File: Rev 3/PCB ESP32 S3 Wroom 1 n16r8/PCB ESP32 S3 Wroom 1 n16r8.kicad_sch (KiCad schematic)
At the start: 28 parts, among them J1 AudioJack3_SwitchT, M1 Haptic Feedback, Q1 BS170, SW1 Home, SW2 Back, SW3 Play/Pause, SW4 Power, SW5 Menu, SW6 Hold, U1 Wemos Lolin32 Lite

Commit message: began work on rev 3
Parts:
- removed U1: Wemos Lolin32 Lite, MP3_Player_Custom_Footprints:Wemos Lolin32 Lite v1.0.0, symbol MP3_Player_Custom_Parts:Wemos Lolin32 Lite
- added X1: ESP32-S3-WROOM-1-N16R8, MP3_Player_Custom_Footprints:ESP32S3WROOM1N8R2, symbol ESP32-S3-WROOM-1-N16R8:ESP32-S3-WROOM-1-N16R8
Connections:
- net GND: now also X1.1 (GND), X1.40 (GND), X1.41 (GND), X1.42 (GND), X1.43 (GND), X1.44 (GND), X1.45 (GND), X1.46 (GND), X1.47 (GND), X1.48 (GND), X1.49 (GND)
- net VDD: now also X1.2 (3V3)

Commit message: wired up ESP32 to the best of my knowledge
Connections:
- net DAC_BCLK: now also X1.5 (IO5)
- net DAC_DIN: now also X1.4 (IO4)
- net DAC_LRC: now also X1.6 (IO6)
- net Detect_Jack: now also X1.15 (IO3)
- net Gain: now also X1.8 (IO15)
- net Motor_Driver: now also X1.11 (IO18)
- net RESET: now also X1.3 (EN)
- net SCREEN_BRIGHTNESS: now also X1.10 (IO17)
- net SD_CS: now also X1.38 (IO2)
- net SPI_MISO: now also X1.20 (IO12)
- net SPI_MOSI: now also X1.21 (IO13)
- net SPI_SCK: now also X1.22 (IO14)
- net TFT_CS: now also X1.39 (IO1)
- net TFT_DC: now also X1.17 (IO9)
- net at Primary Rotary Encoder1.A, R2.1: now also X1.7 (IO7)
- net at R4.2, SW3.2 (B): now also X1.14 (IO20)
- net at X1.12 (IO8): now also SW6.2 (B)
- net at X1.13 (IO19): now also R5.2, R6.2, SW2.1 (A), SW5.2 (B), X1.19 (IO11)
- net at X1.18 (IO10): now also R3.2, SW1.1 (A)
- net at X1.9 (IO16): now also Primary Rotary Encoder1.B, R1.1
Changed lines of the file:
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@@
 	)
 	(junction
+		(at 149.86 72.39)
+		(diameter 0)
+		(color 0 0 0 0)
+	)
+	(junction
 		(at 243.84 129.54)
 		(diameter 0)
@@
 	)
 	(junction
+		(at 149.86 68.58)
+		(diameter 0)
+		(color 0 0 0 0)
+	)
+	(junction
 		(at 149.86 62.23)
 		(diameter 0)
@@
 	(wire
 		(pts
-			(xy 82.55 64.77) (xy 113.03 64.77)
+			(xy 72.39 64.77) (xy 102.87 64.77)
 		)
 		(stroke
@@
 	(wire
 		(pts
-			(xy 160.02 68.58) (xy 195.58 68.58)
+			(xy 149.86 68.58) (xy 195.58 68.58)
 		)
 		(stroke
@@
 	(wire
 		(pts
-			(xy 97.79 85.09) (xy 82.55 85.09)
+			(xy 87.63 85.09) (xy 72.39 85.09)
 		)
 		(stroke
@@
 	(wire
 		(pts
-			(xy 113.03 64.77) (xy 113.03 45.72)
+			(xy 102.87 64.77) (xy 102.87 63.5)
 		)
 		(stroke
@@
 	(wire
 		(pts
-			(xy 139.7 45.72) (xy 139.7 87.63)
+			(xy 129.54 45.72) (xy 129.54 69.85)
 		)
 		(stroke
@@
 	(wire
 		(pts
-			(xy 170.18 73.66) (xy 170.18 95.25)
+			(xy 160.02 73.66) (xy 160.02 95.25)
 		)
 		(stroke
@@
 	(wire
 		(pts
-			(xy 96.52 62.23) (xy 82.55 62.23)
+			(xy 86.36 62.23) (xy 72.39 62.23)
 		)
 		(stroke
@@
 	(wire
 		(pts
-			(xy 97.79 15.24) (xy 228.6 15.24)
+			(xy 87.63 15.24) (xy 228.6 15.24)
 		)
 		(stroke
@@
 	(wire
 		(pts
-			(xy 82.55 90.17) (xy 149.86 90.17)
+			(xy 72.39 72.39) (xy 149.86 72.39)
 		)
 		(stroke
@@
 	(wire
 		(pts
-			(xy 82.55 95.25) (xy 170.18 95.25)
+			(xy 72.39 95.25) (xy 160.02 95.25)
 		)
 		(stroke
@@
 	(wire
 		(pts
-			(xy 170.18 73.66) (xy 203.2 73.66)
+			(xy 160.02 73.66) (xy 203.2 73.66)
 		)
 		(stroke
@@
 	(wire
 		(pts
-			(xy 82.55 92.71) (xy 160.02 92.71)
+			(xy 113.03 63.5) (xy 113.03 45.72)
+		)
+		(stroke
+			(width 0)
+			(type default)
+		)
+	)
+	(wire
+		(pts
+			(xy 72.39 92.71) (xy 149.86 92.71)
 		)
 		(stroke
@@
 	(wire
 		(pts
-			(xy 82.55 87.63) (xy 139.7 87.63)
+			(xy 72.39 69.85) (xy 129.54 69.85)
 		)
 		(stroke
@@
 	(wire
 		(pts
-			(xy 96.52 13.97) (xy 248.92 13.97)
+			(xy 86.36 13.97) (xy 248.92 13.97)
 		)
 		(stroke
@@
 	(wire
 		(pts
-			(xy 149.86 45.72) (xy 139.7 45.72)
+			(xy 149.86 45.72) (xy 129.54 45.72)
 		)
 		(stroke
@@
 	(wire
 		(pts
-			(xy 96.52 13.97) (xy 96.52 62.23)
+			(xy 86.36 13.97) (xy 86.36 62.23)
 		)
 		(stroke
@@
 	(wire
 		(pts
+			(xy 149.86 72.39) (xy 149.86 92.71)
+		)
+		(stroke
+			(width 0)
+			(type default)
+		)
+	)
+	(wire
+		(pts
 			(xy 142.24 135.89) (xy 147.32 135.89)
 		)
@@
 	(wire
 		(pts
-			(xy 160.02 68.58) (xy 160.02 92.71)
+			(xy 149.86 68.58) (xy 149.86 72.39)
 		)
 		(stroke
@@
 	(wire
 		(pts
-			(xy 97.79 15.24) (xy 97.79 85.09)
+			(xy 87.63 15.24) (xy 87.63 85.09)
 		)
 		(stroke
@@
 	(wire
 		(pts
+			(xy 102.87 63.5) (xy 113.03 63.5)
+		)
+		(stroke
+			(width 0)
+			(type default)
+		)
+	)
+	(wire
+		(pts
 			(xy 242.57 25.4) (xy 248.92 25.4)
 		)
@@
 	(wire
 		(pts
-			(xy 149.86 62.23) (xy 149.86 90.17)
+			(xy 228.6 50.8) (xy 228.6 25.4)
 		)
 		(stroke
 			(width 0)
 			(type default)
+			(color 57 191 251 1)
 		)
 	)
 	(wire
 		(pts
-			(xy 228.6 50.8) (xy 228.6 25.4)
+			(xy 149.86 68.58) (xy 149.86 62.23)
 		)
 		(stroke
 			(width 0)
 			(type default)
-			(color 57 191 251 1)
 		)
 	)
@@
 	)
 	(label "SPI_MISO"
-		(at 82.55 69.85 0)
+		(at 72.39 74.93 0)
 		(fields_autoplaced yes)
 		(effects
@@
 	)
 	(label "SPI_MOSI"
-		(at 82.55 77.47 0)
+		(at 72.39 77.47 0)
 		(fields_autoplaced yes)
 		(effects
@@
 	)
 	(label "SD_CS"
-		(at 82.55 49.53 0)
+		(at 72.39 49.53 0)
 		(fields_autoplaced yes)
 		(effects
@@
 	)
 	(label "DAC_LRC"
-		(at 82.55 59.69 0)
+		(at 72.39 59.69 0)
 		(fields_autoplaced yes)
 		(effects
@@
 	)
 	(label "RESET"
-		(at 52.07 36.83 180)
+		(at 39.37 54.61 180)
 		(fields_autoplaced yes)
 		(effects
@@
 	)
 	(label "Gain"
-		(at 82.55 82.55 0)
+		(at 72.39 82.55 0)
 		(fields_autoplaced yes)
 		(effects
@@
 	)
 	(label "SCREEN_BRIGHTNESS"
-		(at 82.55 80.01 0)
+		(at 72.39 87.63 0)
 		(fields_autoplaced yes)
 		(effects
@@
 	)
 	(label "TFT_CS"
-		(at 82.55 46.99 0)
+		(at 72.39 46.99 0)
 		(fields_autoplaced yes)
 		(effects
@@
 	)
 	(label "DAC_DIN"
-		(at 82.55 54.61 0)
+		(at 72.39 54.61 0)
 		(fields_autoplaced yes)
 		(effects
@@
 	)
 	(label "DAC_BCLK"
-		(at 82.55 57.15 0)
+		(at 72.39 57.15 0)
 		(fields_autoplaced yes)
 		(effects
@@
 	)
 	(label "Detect_Jack"
-		(at 82.55 52.07 0)
+		(at 72.39 52.07 0)
 		(fields_autoplaced yes)
 		(effects
@@
 	)
 	(label "SPI_SCK"
-		(at 82.55 67.31 0)
+		(at 72.39 80.01 0)
 		(fields_autoplaced yes)
 		(effects
@@
 	)
 	(label "TFT_DC"
-		(at 82.55 41.91 0)
+		(at 72.39 67.31 0)
 		(fields_autoplaced yes)
 		(effects
@@
 	)
 	(label "Motor_Driver"
-		(at 82.55 74.93 0)
+		(at 72.39 90.17 0)
 		(fields_autoplaced yes)
 		(effects
@@
 		(on_board yes)
 		(dnp no)
-		(fields_autoplaced yes)
 		(property "Reference" "#PWR014"
 			(at 33.02 46.99 0)
@@
 		)
 		(property "Value" "GND"
-			(at 38.1 43.18 90)
+			(at 40.64 48.26 90)
 			(effects
 				(font

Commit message: added datasheet
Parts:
- added R8: 10K, Resistor_THT:R_Axial_DIN0204_L3.6mm_D1.6mm_P7.62mm_Horizontal, symbol Device:R
- added SW7: BOOT_MODE, symbol Switch:SW_Push
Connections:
- net GND: now also SW7.1
- net VDD: now also R8.1
- net at R4.2, SW3.2 (B): no longer X1.14 (IO20)
- net at R5.2, R6.2, SW2.1 (A)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: no longer X1.13 (IO19)
- net at X1.27 (IO0): now also R8.2, SW7.2

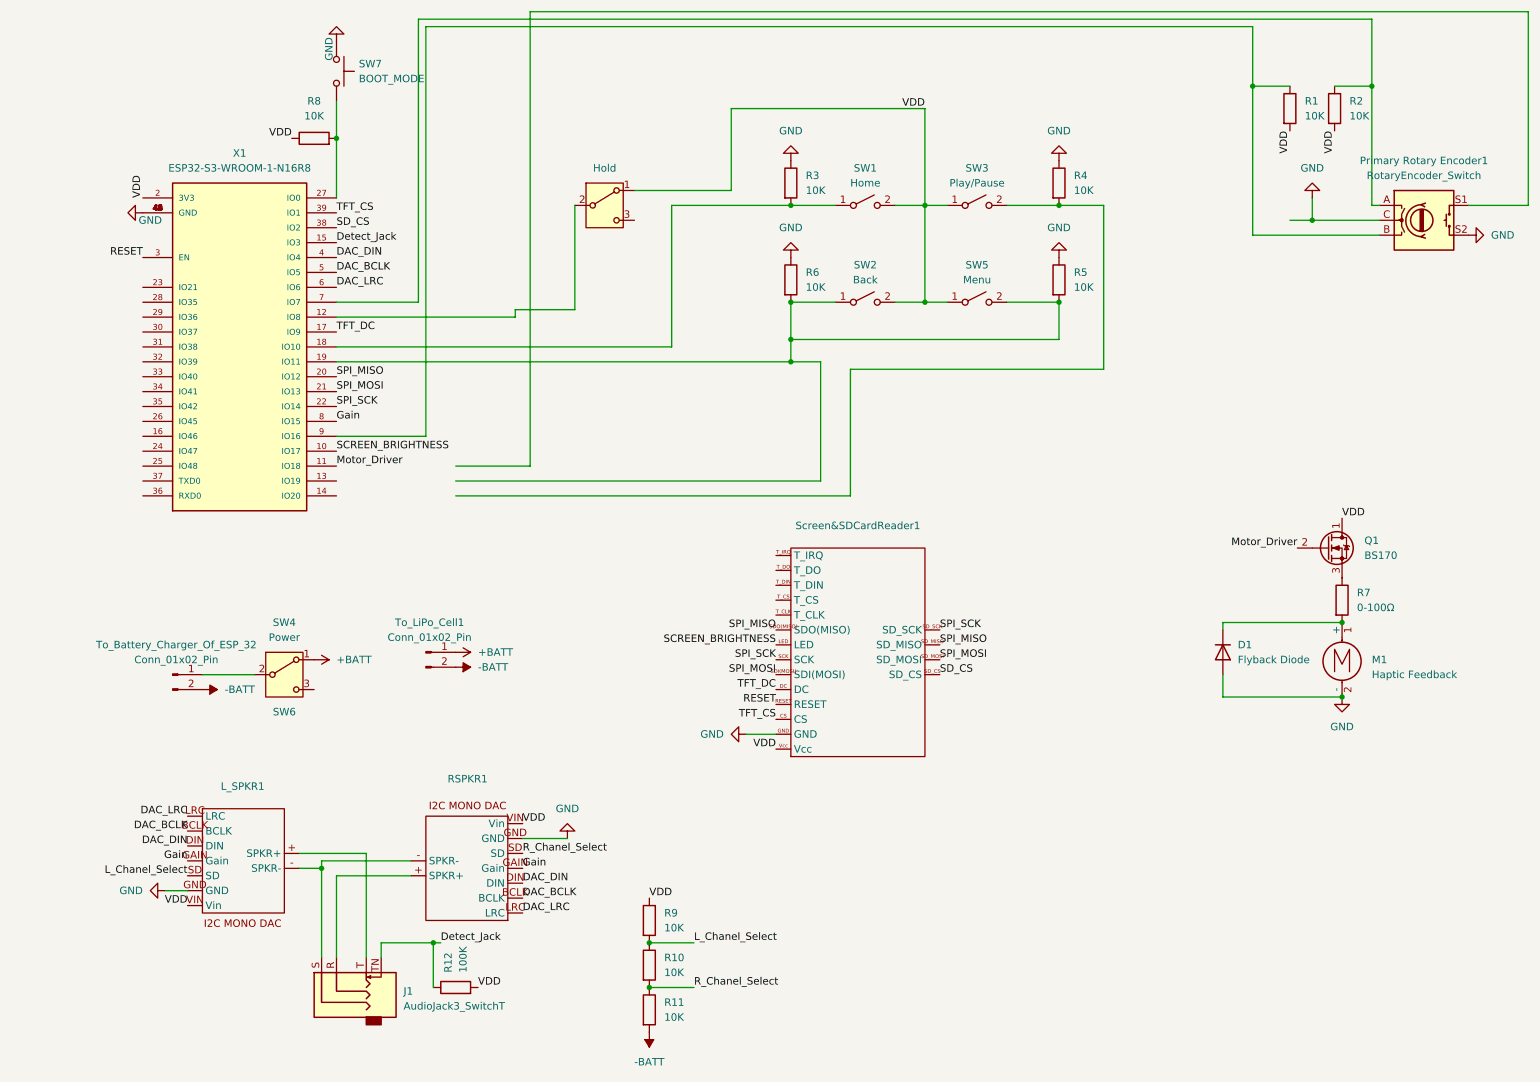
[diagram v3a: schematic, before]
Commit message: updated schematic using datasheet
- checked documentation on all pins
- added FTDI header, minus 5V to 3v3 Regulator
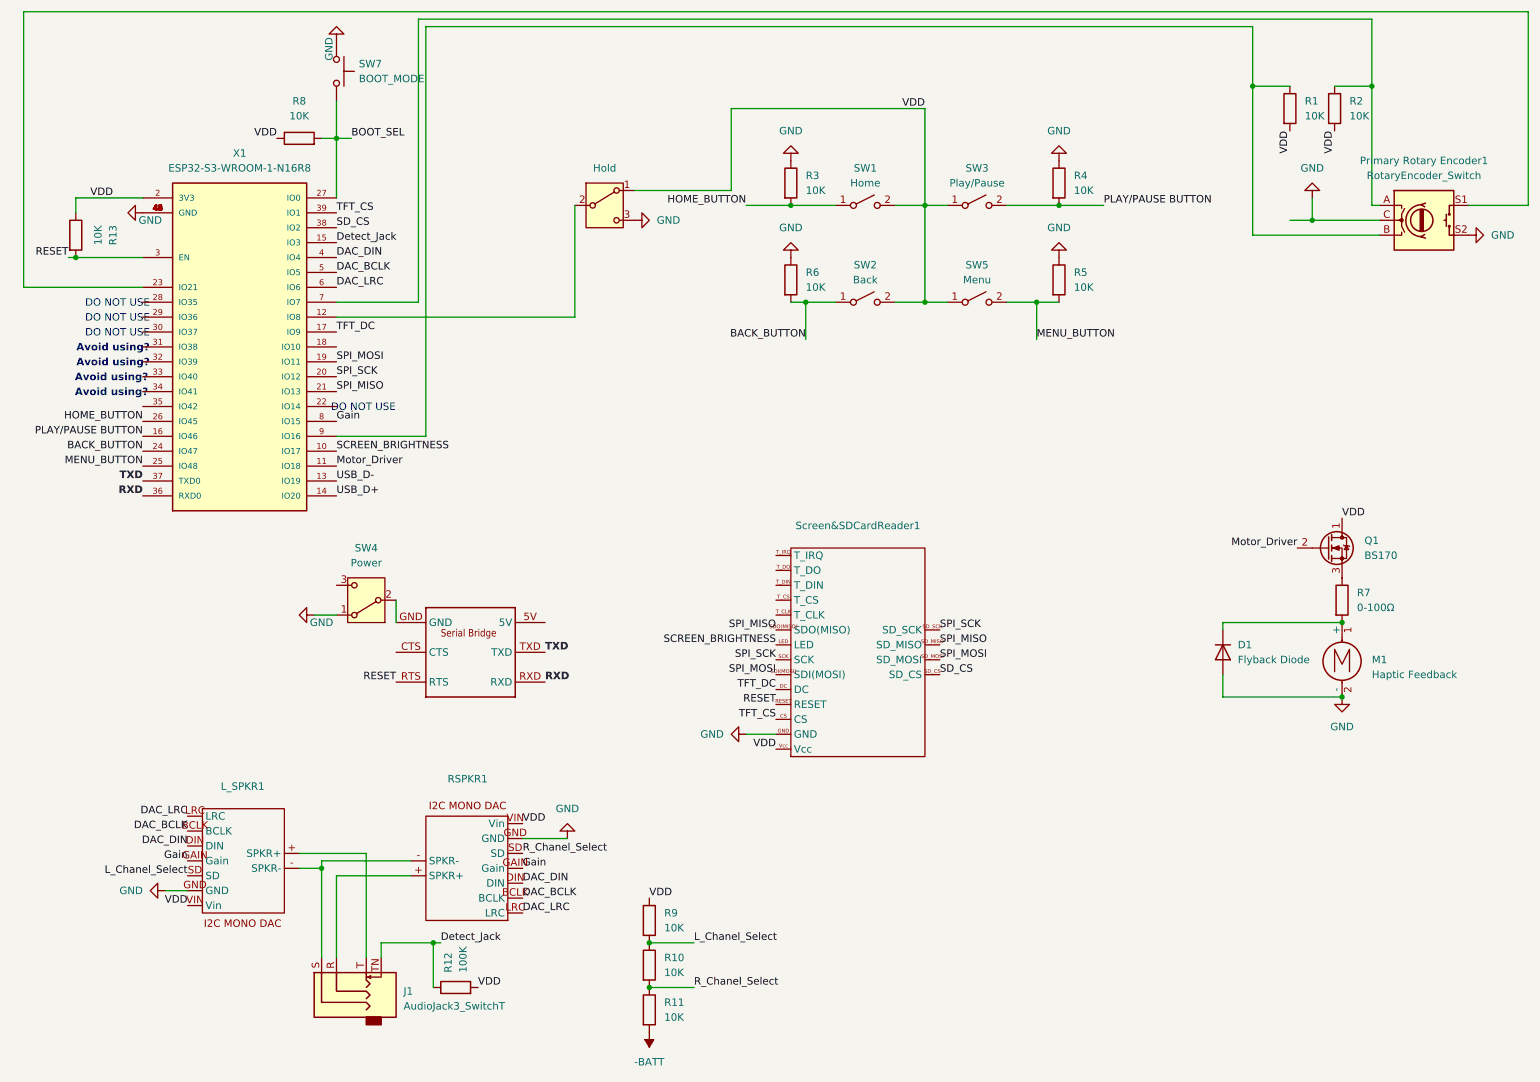
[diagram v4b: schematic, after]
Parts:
- removed To_Battery_Charger_Of_ESP_32, To_LiPo_Cell1: Conn_01x02_Pin, Connector_JST:JST_XA_B02B-XASK-1-A_1x02_P2.50mm_Vertical, symbol Connector:Conn_01x02_Pin
- added 1: ~, ESP32 camera and friends:UART_FTDI, symbol MP3_Player_Custom_Parts:UART_FTDI
- added R13: 10K, Resistor_THT:R_Axial_DIN0204_L3.6mm_D1.6mm_P7.62mm_Horizontal, symbol Device:R
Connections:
- net +BATT is gone; now on net GND: SW4.1 (A)
- net GND: now also SW6.3 (C)
- net RESET: now also 1.RTS, R13.2
- net SPI_MISO: now also X1.21 (IO13); no longer X1.20 (IO12)
- net SPI_MOSI: now also X1.19 (IO11); no longer X1.21 (IO13)
- net SPI_SCK: now also X1.20 (IO12); no longer X1.22 (IO14)
- net VDD: now also R13.1
- net PLAY/PAUSE BUTTON: now reaches R4.2, SW3.2 (B)
- net PLAY/PAUSE BUTTON: now also X1.16 (IO46)
- net USB_D-: now reaches X1.13 (IO19)
- net USB_D+: now reaches X1.14 (IO20)
- net HOME_BUTTON: now reaches R3.2, SW1.1 (A)
- net HOME_BUTTON: now also X1.26 (IO45); no longer X1.18 (IO10)
- net at X1.23 (IO21): now also Primary Rotary Encoder1.S1
- net BACK_BUTTON: now reaches X1.24 (IO47)
- net BACK_BUTTON: now also R6.2, SW2.1 (A)
- net MENU_BUTTON: now reaches X1.25 (IO48)
- net MENU_BUTTON: now also R5.2, SW5.2 (B)
- net BOOT_SEL: now reaches R8.2, SW7.2, X1.27 (IO0)
- net RXD: now reaches X1.36 (RXD0)
- net RXD: now also 1.RXD
- net TXD: now reaches X1.37 (TXD0)
- net TXD: now also 1.TXD
- net at SW4.2 (B): now also 1.GND
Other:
- note added: "Avoid using?"
- note added: "DO NOT USE"
- moved on the sheet: R8, SW4

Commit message: Renamed Sheet
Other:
- title: (none) -> BYU IEEE MP3 Player 2024-2025
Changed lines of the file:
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@@
 	(generator_version "8.0")
 	(paper "A4")
+	(title_block
+		(title "BYU IEEE MP3 Player 2024-2025")
+		(rev "3")
+	)
 	(junction
 		(at 69.85 158.75)

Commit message: Added More 3d Models
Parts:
- 1: footprint ESP32 camera and friends:UART_FTDI -> (none)
- SW7: footprint (none) -> MP3_Player_Custom_Footprints:UART_FTDI
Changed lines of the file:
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@@
 			)
 		)
-		(property "Footprint" ""
+		(property "Footprint" "MP3_Player_Custom_Footprints:UART_FTDI"
 			(at 77.47 22.86 0)
 			(effects
@@
 			)
 		)
-		(property "Footprint" "ESP32 camera and friends:UART_FTDI"
+		(property "Footprint" ""
 			(at 95.504 112.776 0)
 			(effects
